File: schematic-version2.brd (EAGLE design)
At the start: 47 x 28 mm, 56 parts, among them J1 FTDI_DEVICERA_SMT, M1 WIRELESS-NRF24L01, Q1 8MHz, T1 NMOS, T2 NMOS, T3 NMOS, T4 NMOS, U1 ATMEGA328P_TQFP, U2 GY-521MPU6050, U3 LTC3534

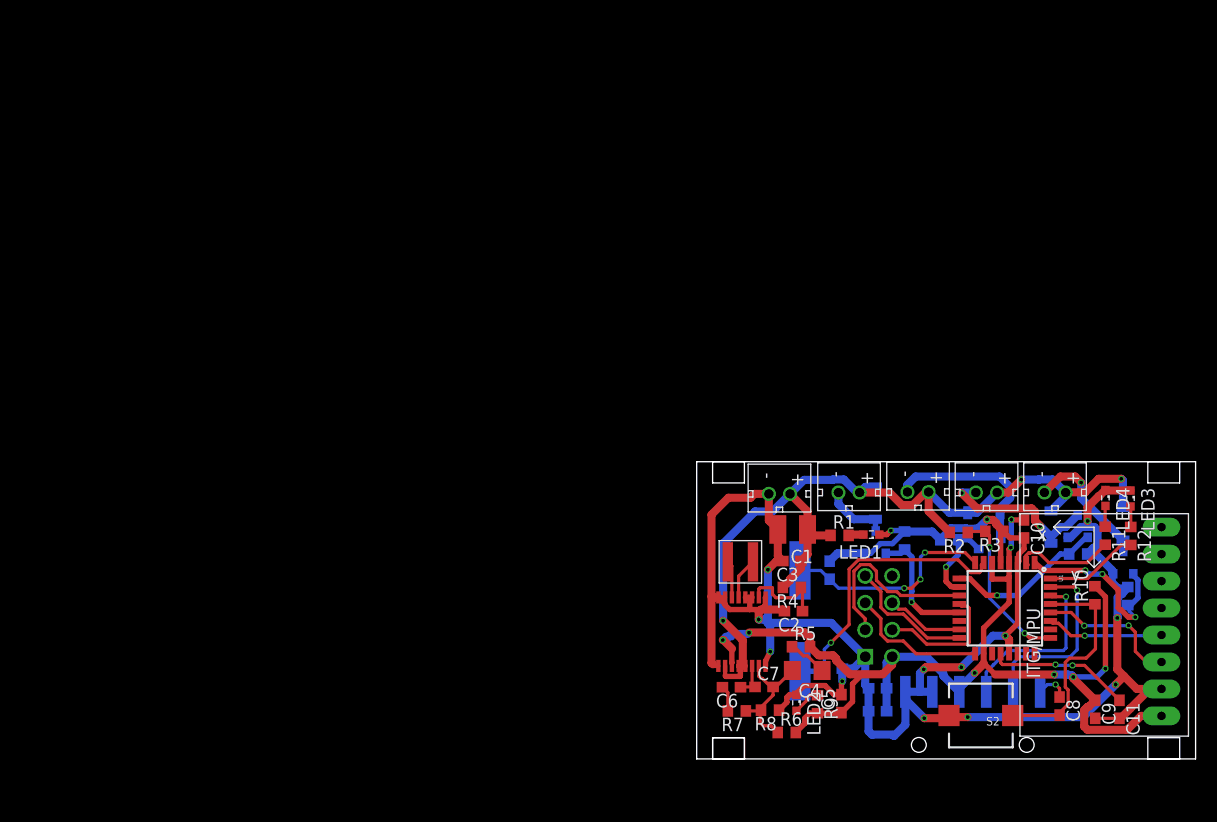
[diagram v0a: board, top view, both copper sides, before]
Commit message: Made some changes according to review notes
Fixed FTDI connector, added keepout outline to voltage regulator. Changes are reflected in version2 file. version2 board is empty for you routing pleasure.
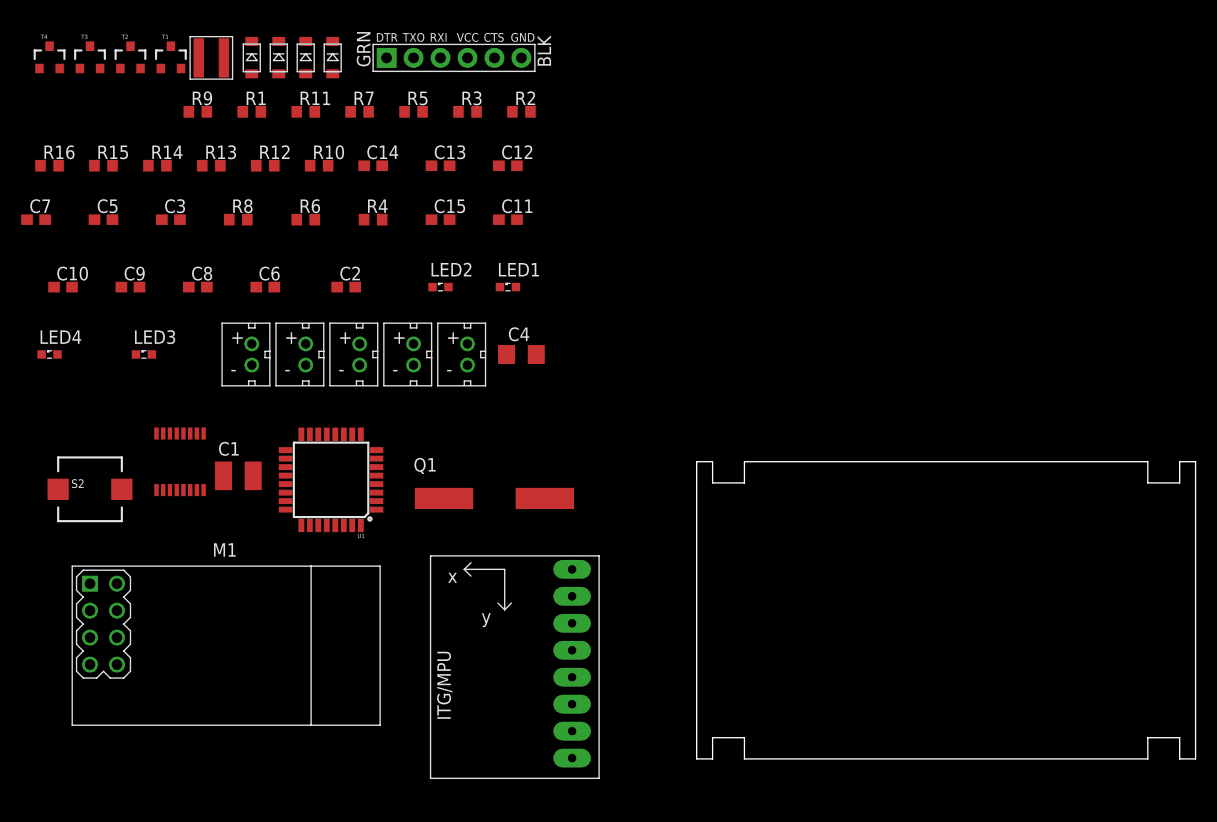
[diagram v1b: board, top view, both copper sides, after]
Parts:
- removed J1: FTDI_DEVICERA_SMT, quad:FTDI_DEVICE_RA_SMT
- removed U3: LTC3534, LTC3534:SSOP-16GN
- added J2: FTDI_DEVICE, quad:FTDI_DEVICE_SIDE
- added U$2: LTC3534, LTC3534:SSOP-16GN
- moved T1 101.6 mm to (-49.5, 66.0), flipped to the top
- moved LED4 100.4 mm to (-61.0, 38.1), turned to 0 degrees
- moved T2 99.6 mm to (-53.3, 66.0), flipped to the top
- moved C9 99.2 mm to (-53.3, 44.5), turned to 0 degrees
- moved T3 96.1 mm to (-57.1, 66.0), flipped to the top, turned to 0 degrees
- moved R13 95.4 mm to (-45.7, 55.9), flipped to the top, turned to 0 degrees
- moved R14 94.1 mm to (-50.8, 55.9), flipped to the top
- moved LED3 93.9 mm to (-52.1, 38.1), turned to 0 degrees
- moved C10 93.3 mm to (-59.7, 44.5), turned to 0 degrees
- moved C8 90.3 mm to (-47.0, 44.5), turned to 0 degrees
- moved T4 90.2 mm to (-61.0, 66.0), flipped to the top
- moved R12 88.7 mm to (-40.6, 55.9), turned to 0 degrees
- moved R16 87.9 mm to (-61.0, 55.9), flipped to the top, turned to 0 degrees
- moved R15 87.1 mm to (-55.9, 55.9), flipped to the top, turned to 0 degrees
- moved S2 86.6 mm to (-57.1, 25.4), turned to 0 degrees
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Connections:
- net DTR: now also J2.P$1; no longer J1.1
- net GND: now also J2.P$5, J2.P$6, U$2.1, U$2.16, U$2.3, U$2.4, U$2.7, U$2.8, U$2.9; no longer J1.5, J1.6, U3.1, U3.16, U3.3, U3.4, U3.7, U3.8, U3.9
- net N$16: now also U$2.2; no longer U3.2
- net N$18: now also U$2.15; no longer U3.15
- net N$19: now also U$2.14; no longer U3.14
- net N$8: now also U$2.5; no longer U3.5
- net N$9: now also U$2.6; no longer U3.6
- net PWR: now also U$2.10, U$2.12, U$2.13; no longer U3.10, U3.12, U3.13
- net RXD: now also J2.P$3; no longer J1.3
- net TXD: now also J2.P$2; no longer J1.2
- net V_REG_OUT: now also J2.P$4, U$2.11; no longer J1.4, U3.11
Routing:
- net GND: track 205.7 -> 0.00 mm, vias 14 -> 0
- net V_REG_OUT: track 110.1 -> 0.00 mm, vias 8 -> 0
- net PWR: track 85.1 -> 0.00 mm, vias 3 -> 0
- net N$1: track 27.0 -> 0.00 mm, vias 1 -> 0
- net N$2: track 21.6 -> 0.00 mm
- net N$4: track 20.2 -> 0.00 mm, vias 3 -> 0
- net PWM1: track 18.1 -> 0.00 mm, vias 3 -> 0
- net CE: track 17.8 -> 0.00 mm
- net TXD: track 17.5 -> 0.00 mm, vias 1 -> 0
- net RXD: track 16.7 -> 0.00 mm, vias 1 -> 0
- net N$5: track 16.5 -> 0.00 mm, vias 2 -> 0
- net N$6: track 16.4 -> 0.00 mm
- net V_BAT: track 15.4 -> 0.00 mm, vias 2 -> 0
- net PWM2: track 15.0 -> 0.00 mm, vias 1 -> 0
- net N$25: track 13.5 -> 0.00 mm, vias 2 -> 0
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
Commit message: Oops
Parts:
- moved U2 5.57 mm to (-25.8, 6.93)
- moved M1 3.09 mm to (-47.5, 9.80), flipped to the bottom, turned to 180 degrees
- moved U$2 1.66 mm to (-49.5, 26.5)
- moved U1 1.27 mm to (-33.7, 25.3)
